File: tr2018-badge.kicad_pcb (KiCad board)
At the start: 2 copper layers, 70.4 x 53.3 mm, 16 parts, among them U1 ESP-12F, X1 Badgelife_shitty_connector

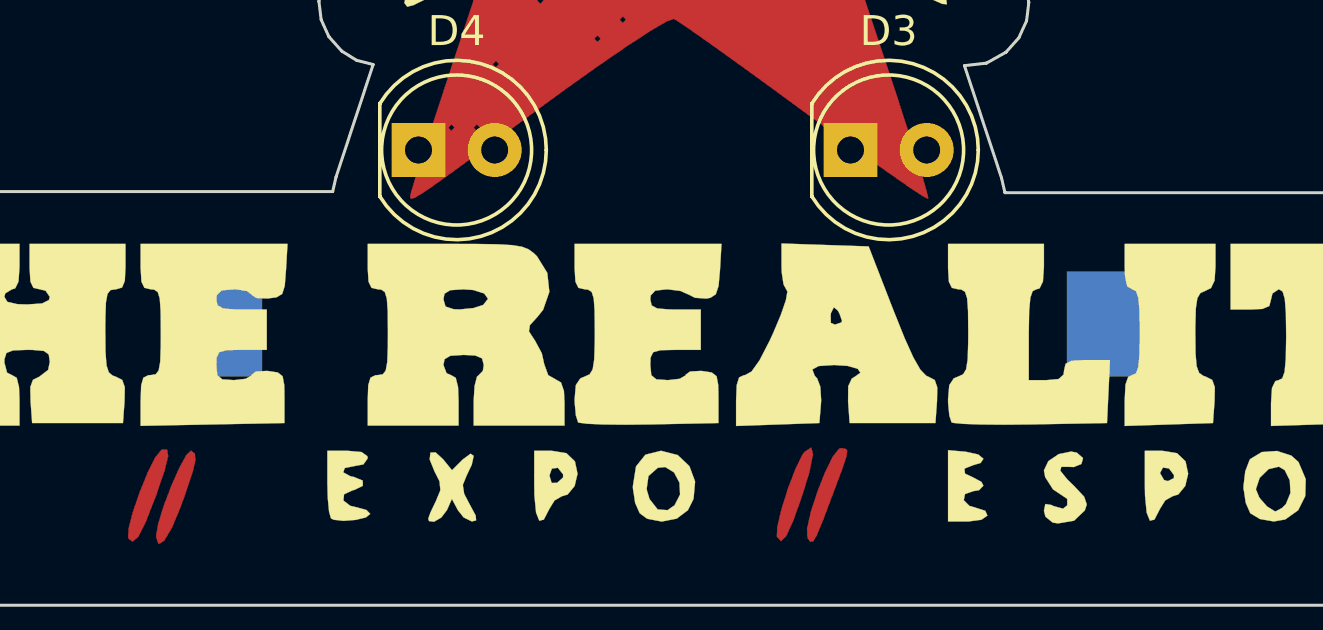
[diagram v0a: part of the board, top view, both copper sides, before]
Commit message: Updated schematic & design, added costs spreadsheet
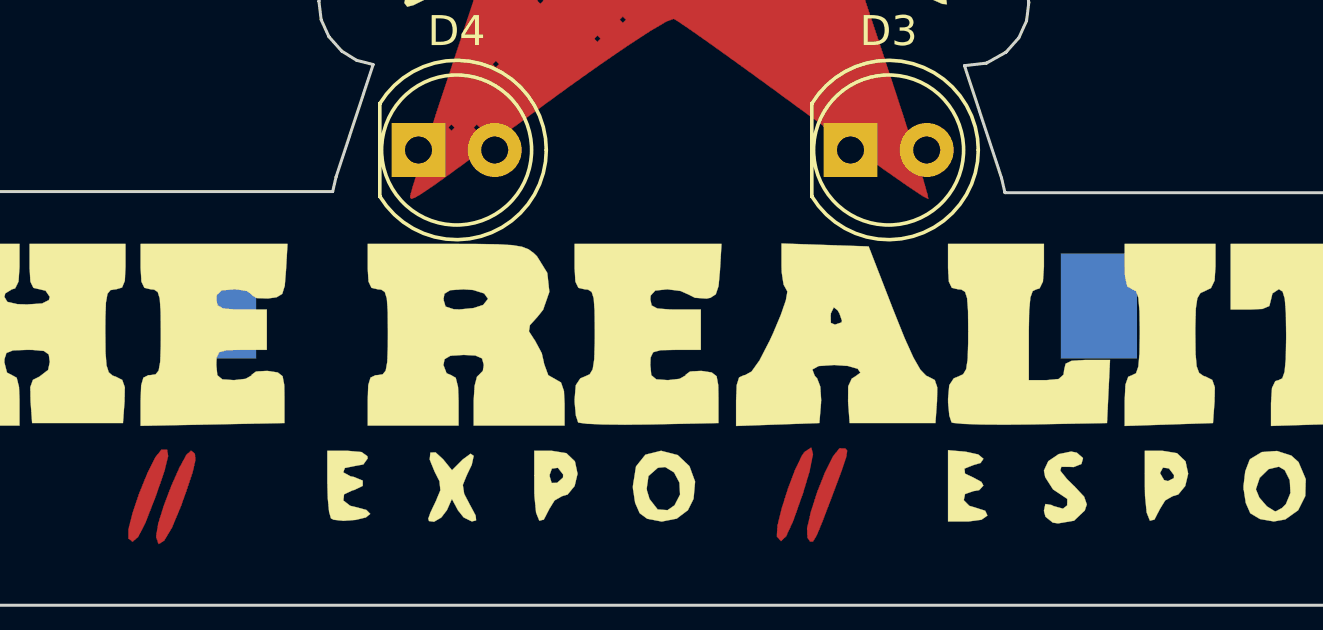
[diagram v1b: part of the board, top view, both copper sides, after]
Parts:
- moved BT1 0.63 mm to (52.0, 60.2)
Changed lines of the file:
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@@
     (pad_to_mask_clearance 0.2)
     (aux_axis_origin 0 0)
-    (visible_elements FFFFFF7F)
+    (visible_elements 7FFFFFFF)
     (pcbplotparams
       (layerselection 0x00030_80000001)
@@
   )
   (module Battery_Holders:Keystone_1058_1x2032-CoinCell (layer B.Cu)
-    (at 52.2 60.8 180)
+    (at 52 60.2 180)
     (descr http://www.keyelco.com/product-pdf.cfm?p=14028)
     (tags "Keystone type 1058 coin cell retainer")

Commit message: Added notes on PCB layout
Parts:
- D1: footprint LEDs:LED_D5.0mm -> LEDs:LED_D3.0mm
- moved D2 107.3 mm to (157.8, 91.4)
- moved D1 107.3 mm to (145.6, 82.4)
- moved R1 107.3 mm to (147.0, 84.4)
- moved R2 107.3 mm to (147.0, 86.2)
- moved R3 107.3 mm to (147.0, 88.0)
- moved U1 107.3 mm to (136.2, 81.0)
- moved X1 107.3 mm to (171.8, 113.0)
- moved BT1 107.3 mm to (146.6, 110.8)
- moved D3 107.3 mm to (153.0, 105.6)
- moved D4 107.3 mm to (138.6, 105.6)
- moved D5 107.3 mm to (134.2, 91.6)
- moved G*** 107.3 mm to (147.0, 94.6)
- moved G*** 107.3 mm to (147.0, 94.8)
- moved R4 107.3 mm to (147.0, 89.8)
- moved R5 107.3 mm to (147.0, 91.6)
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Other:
- board text added: "TODO: - Add version number on PCB - Add HackZone logo somewhere - Add names of contributors"

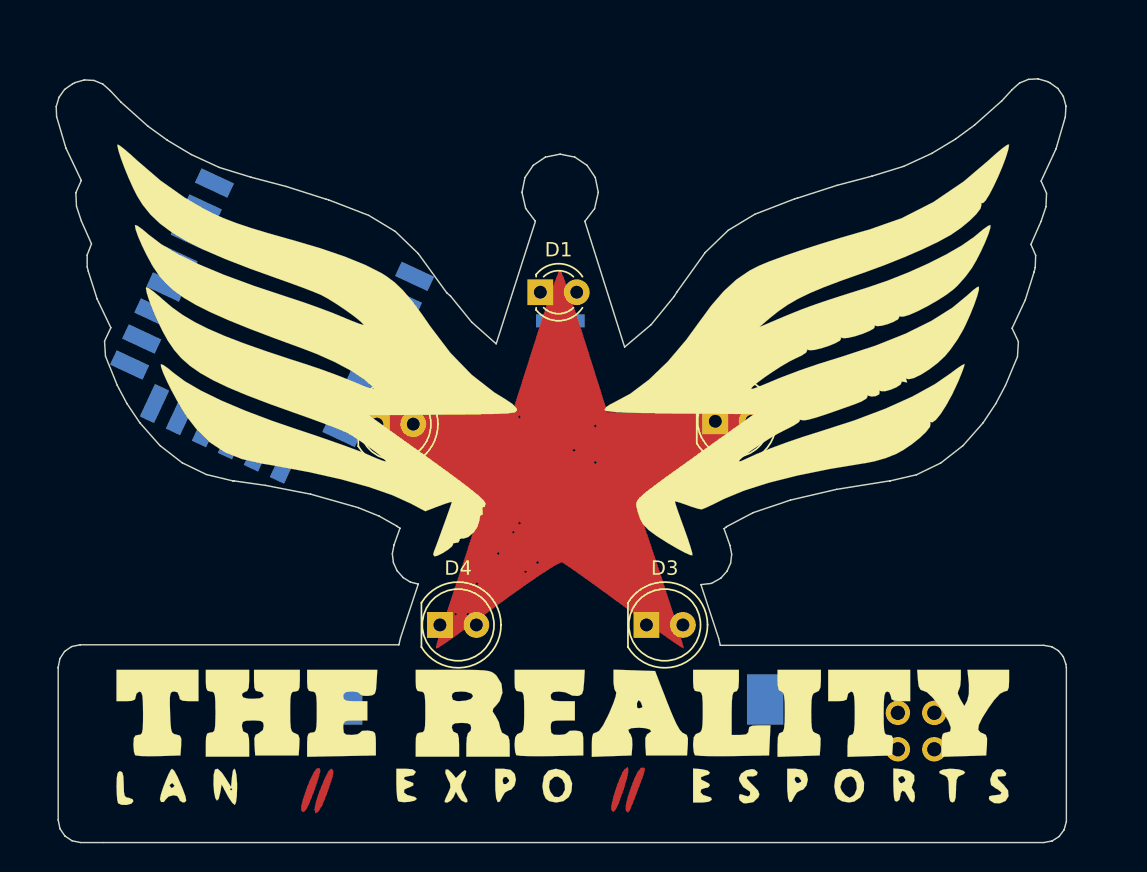
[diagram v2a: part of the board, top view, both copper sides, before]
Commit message: Updated badge design with latest ideas
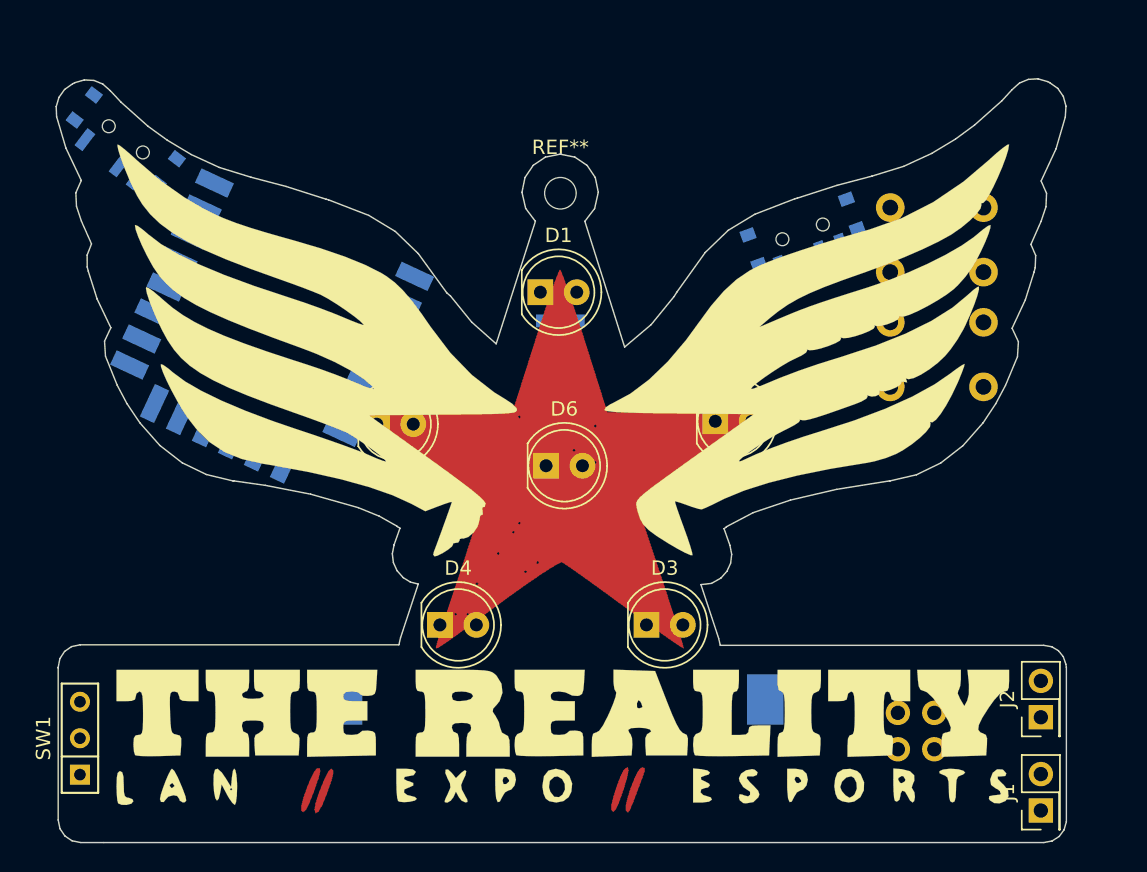
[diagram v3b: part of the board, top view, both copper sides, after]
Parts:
- added D6: LED, LEDs:LED_D5.0mm, F.Cu at (146.0, 94.5)
- added J1: Conn_02x01_Row_Letter_First, Pin_Headers:Pin_Header_Straight_2x01_Pitch2.54mm, F.Cu at (180.5, 118.5)
- added J2: Conn_02x01_Row_Letter_First, Pin_Headers:Pin_Header_Straight_2x01_Pitch2.54mm, F.Cu at (180.5, 112.0)
- added REF**: MountingHole_2.2mm_M2, Mounting_Holes:MountingHole_2.2mm_M2, F.Cu at (147.0, 75.5)
- added SW1: SW_SPDT, Buttons_Switches_THT:SW_Micro_SPST, F.Cu at (113.5, 113.5)
- added SW2: SW_SPDT, Buttons_Switches_SMD:SW_SPDT_PCM12, B.Cu at (116.5, 72.0)
- added SW3: SW_Push, Buttons_Switches_THT:SW_PUSH_6mm_h4.3mm, B.Cu at (176.5, 84.5)
- added SW4: SW_Push, Buttons_Switches_THT:SW_PUSH_6mm_h4.3mm, B.Cu at (170.0, 81.0)
- added SW5: SW_SPDT, Buttons_Switches_SMD:SW_SPDT_PCM12, B.Cu at (164.0, 78.5)
- D1: footprint LEDs:LED_D3.0mm -> LEDs:LED_D5.0mm
- renumbered G*** to COPPER, G*** to SILK
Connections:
- BT1 pad 2: GND -> Net-(BT1-Pad2)
- U1 pad 15: Net-(U1-Pad15) -> (no net)
- U1 pad 16: Net-(U1-Pad16) -> (no net)
- U1 pad 17: Net-(U1-Pad17) -> (no net)
- U1 pad 18: Net-(U1-Pad18) -> (no net)
- U1 pad 19: Net-(U1-Pad19) -> (no net)
- U1 pad 2: Net-(U1-Pad2) -> (no net)
- U1 pad 20: Net-(U1-Pad20) -> (no net)
- U1 pad 21: Net-(U1-Pad21) -> (no net)
- U1 pad 22: Net-(U1-Pad22) -> (no net)
- U1 pad 4: Net-(U1-Pad4) -> (no net)
- U1 pad 5: Net-(U1-Pad5) -> (no net)
- U1 pad 6: Net-(U1-Pad6) -> (no net)
- U1 pad 7: Net-(U1-Pad7) -> (no net)

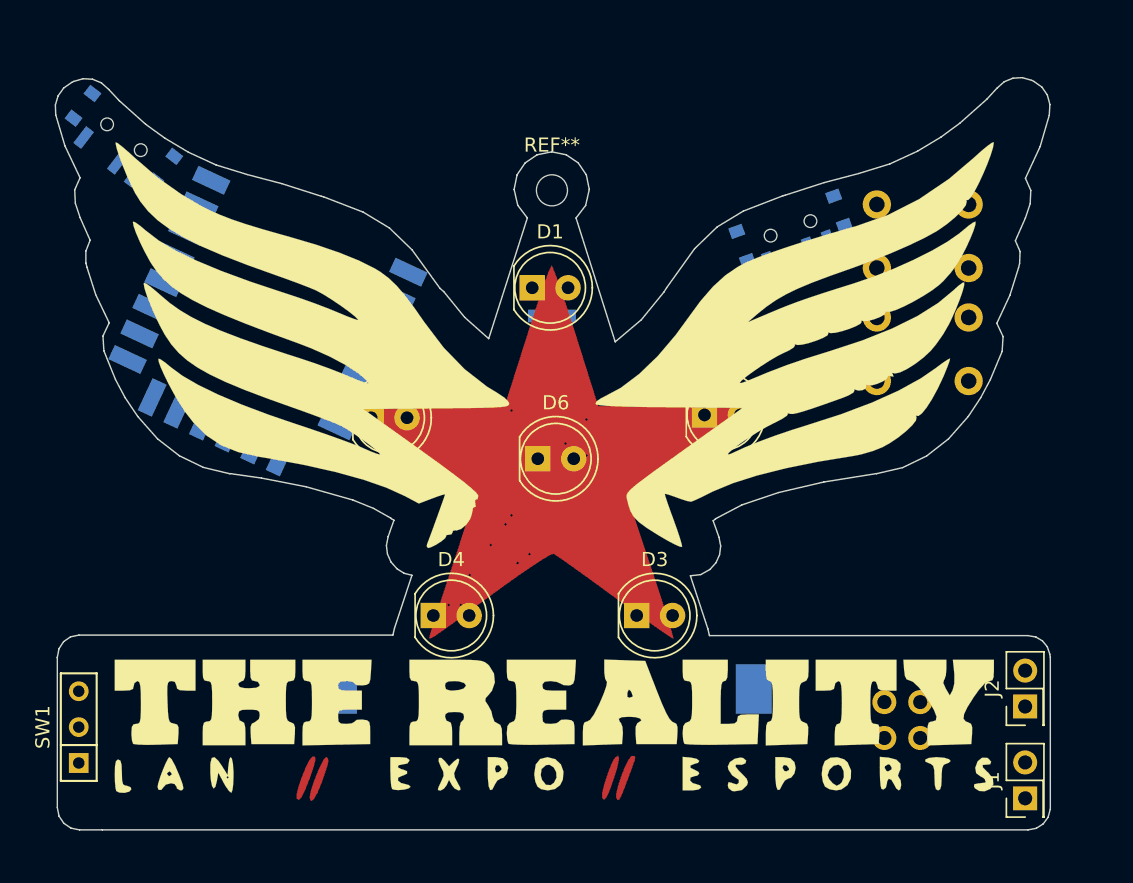
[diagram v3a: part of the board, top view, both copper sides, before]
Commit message: Design for PCB mill prototype (w/o functional ESP + SAO)
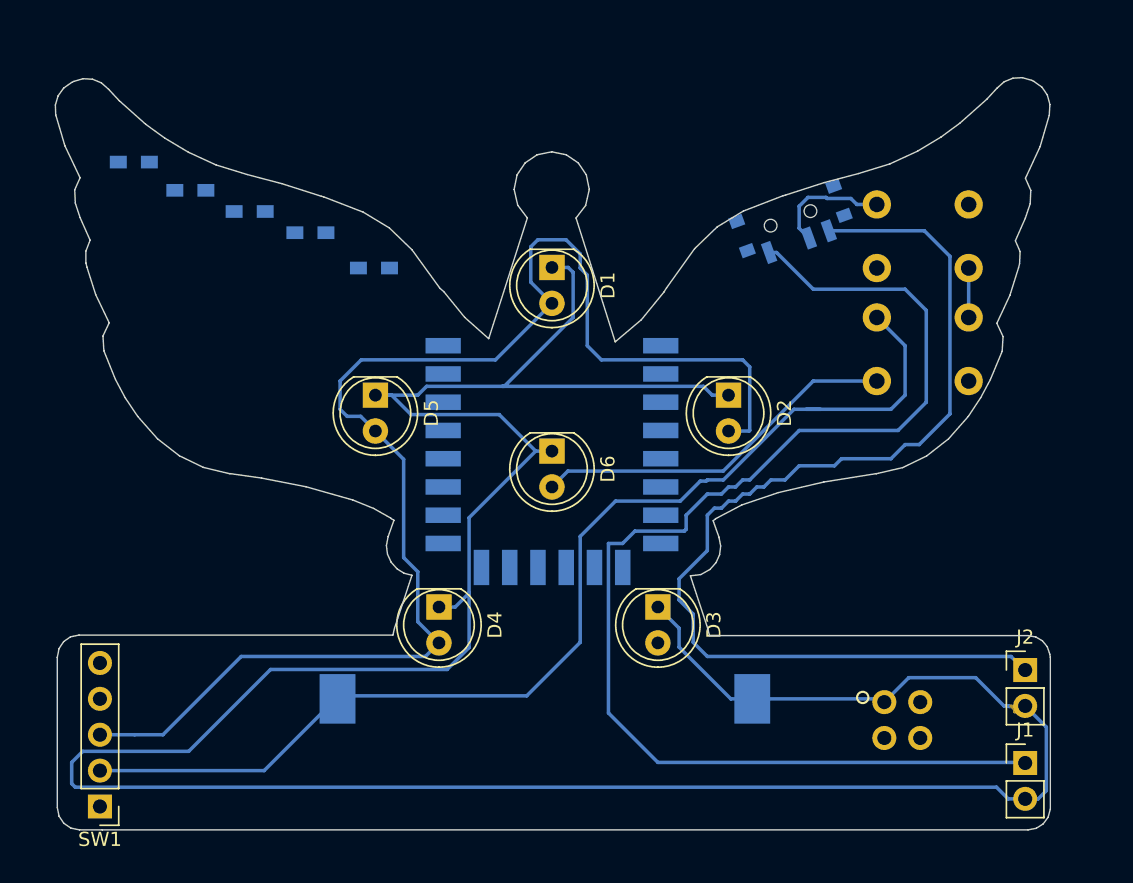
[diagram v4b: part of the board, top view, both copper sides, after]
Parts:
- removed COPPER: LOGO, modules:fill_cu
- removed REF**: MountingHole_2.2mm_M2, Mounting_Holes:MountingHole_2.2mm_M2
- removed SILK: LOGO, modules:wingstext
- removed STAR: LOGO, modules:fill
- removed SW2: SW_SPDT, Buttons_Switches_SMD:SW_SPDT_PCM12
- J1, J2: value Conn_02x01_Row_Letter_First -> Conn_01x02; footprint Pin_Headers:Pin_Header_Straight_2x01_Pitch2.54mm -> Pin_Headers:Pin_Header_Straight_1x02_Pitch2.54mm
- SW1: footprint Buttons_Switches_THT:SW_Micro_SPST -> Pin_Headers:Pin_Header_Straight_1x05_Pitch2.54mm
- moved R5 34.7 mm to (117.4, 73.5), turned to 180 degrees
- moved R4 29.3 mm to (121.4, 75.5), turned to 180 degrees
- moved R3 24.1 mm to (125.6, 77.0), turned to 180 degrees
- moved R2 18.8 mm to (129.9, 78.5), turned to 180 degrees
- moved U1 18.6 mm to (154.0, 86.5), turned to 180 degrees
- moved R1 13.1 mm to (134.4, 81.0)
- moved SW1 5.82 mm to (115.0, 119.1), turned to 180 degrees
- moved J2 2.58 mm to (180.5, 109.5), turned to 0 degrees
- moved J1 2.50 mm to (180.5, 116.0), turned to 0 degrees
- moved D2 2.20 mm to (159.5, 90.0), turned to 270 degrees
- moved D1 2.01 mm to (147.0, 81.0), turned to 270 degrees
- moved D5 1.63 mm to (134.5, 90.0), turned to 270 degrees
- moved D3 1.62 mm to (154.5, 105.0), turned to 270 degrees
- moved D6 1.14 mm to (147.0, 94.0), turned to 270 degrees
- moved D4 0.72 mm to (139.0, 105.0), turned to 270 degrees
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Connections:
- BT1 pad 2: Net-(BT1-Pad2) -> GND
- D1 pad 2: GND -> Net-(D1-Pad2)
- D2 pad 2: GND -> Net-(D1-Pad2)
- D3 pad 2: GND -> Net-(D1-Pad2)
- D4 pad 2: GND -> Net-(D1-Pad2)
- D5 pad 2: GND -> Net-(D1-Pad2)
- J1 pad 1: (no net) -> Net-(J1-Pad1)
- J1 pad 2: (no net) -> VCC
- J2 pad 1: (no net) -> Net-(J2-Pad1)
- J2 pad 2: (no net) -> VCC
- SW1 pad 2: Net-(SW1-Pad2) -> GND
- SW1 pad 3: Net-(BT1-Pad2) -> Net-(D1-Pad2)
- SW5 pad 1: (no net) -> Net-(J1-Pad1)
- SW5 pad 3: (no net) -> Net-(J2-Pad1)
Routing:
- net VCC: track 0.00 -> 210.4 mm
- net Net-(D1-Pad2): track 0.00 -> 99.6 mm
- net Net-(J1-Pad1): track 0.00 -> 89.5 mm
- net GND: track 0.00 -> 83.2 mm
- net Net-(J2-Pad1): track 0.00 -> 75.2 mm
- net Net-(D6-Pad2): track 0.00 -> 26.1 mm
- net Net-(SW4-Pad2): track 0.00 -> 8.50 mm
- net (no net): track 0.00 -> 0.72 mm

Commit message: Bump to rev 1.0.0
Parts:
- added G***: LOGO, modules:fill_mask, F.Cu at (147.0, 94.0)
- added REF**: MountingHole_2.2mm_M2_Pad_Via, Mounting_Holes:MountingHole_2.2mm_M2_Pad_Via, F.Cu at (147.0, 75.5)
- added Wings: LOGO, modules:wingstext, F.Cu at (147.0, 94.0)
- BT1: footprint Battery_Holders:Keystone_1058_1x2032-CoinCell -> BatteryHolder:Keystone_1058_1x2032-CoinCell
- J1, J2: moved to B.Cu
- R5: value 10k -> 10k (all opt.)
- SW1: footprint Pin_Headers:Pin_Header_Straight_1x05_Pitch2.54mm -> modules:SW_CuK_OS102011MA1QN1_SPDT_Angled; moved to B.Cu
- SW5 (opt.): renamed from SW5
- U1: value ESP-12F -> ESP-12F (opt.)
- X1: value Badgelife_shitty_connector -> Defcon Shitty AddOn (opt.) >
- moved X1 60.9 mm to (119.2, 82.3)
- moved SW1 43.7 mm to (124.2, 76.4), turned to 344 degrees
- moved J1 35.6 mm to (165.0, 84.0), turned to 90 degrees
- moved J2 26.9 mm to (165.0, 87.5), turned to 90 degrees
- moved R4 16.4 mm to (122.5, 91.9), turned to 270 degrees
- moved R5 15.2 mm to (119.5, 88.6), turned to 270 degrees
- moved R3 14.9 mm to (125.0, 91.9), turned to 270 degrees
- moved R2 13.6 mm to (127.5, 91.9), turned to 90 degrees
- moved R1 11.8 mm to (130.0, 91.9), turned to 90 degrees
- moved D4 0.50 mm to (139.5, 105.0)
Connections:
- SW1 pad 1: (no net) -> Net-(SW1-Pad1)
- U1 pad 15: (no net) -> Net-(U1-Pad15)
- U1 pad 16: (no net) -> Net-(U1-Pad16)
- U1 pad 17: (no net) -> Net-(U1-Pad17)
- U1 pad 18: (no net) -> Net-(U1-Pad18)
- U1 pad 19: (no net) -> Net-(U1-Pad19)
- U1 pad 2: (no net) -> Net-(U1-Pad2)
- U1 pad 20: (no net) -> Net-(U1-Pad20)
- U1 pad 21: (no net) -> Net-(U1-Pad21)
- U1 pad 22: (no net) -> Net-(U1-Pad22)
- U1 pad 4: (no net) -> Net-(U1-Pad4)
- U1 pad 5: (no net) -> Net-(U1-Pad5)
- U1 pad 6: (no net) -> Net-(U1-Pad6)
- U1 pad 7: (no net) -> Net-(U1-Pad7)
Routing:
- net Net-(J1-Pad1): track 89.5 -> 5.20 mm
- net VCC: track 210.4 -> 132.3 mm, vias 0 -> 1
- net Net-(J2-Pad1): track 75.2 -> 9.80 mm
- net GND: track 83.2 -> 126.2 mm, vias 0 -> 3
- net Net-(R1-Pad1): track 0.00 -> 32.7 mm, vias 0 -> 2
- net SDA: track 0.00 -> 30.8 mm, vias 0 -> 3
- net Net-(R2-Pad1): track 0.00 -> 29.6 mm
- net SCL: track 0.00 -> 26.4 mm, vias 0 -> 3
- net Net-(R5-Pad2): track 0.00 -> 24.9 mm, vias 0 -> 2
- net Net-(D1-Pad2): track 99.6 -> 76.8 mm, vias 0 -> 3
- net Net-(D6-Pad2): track 26.1 -> 48.4 mm, vias 0 -> 1
- net Net-(R4-Pad2): track 0.00 -> 18.9 mm
- net FLASH_EN: track 0.00 -> 17.1 mm
- net Net-(SW4-Pad2): track 8.50 -> 14.8 mm
- net (no net): track 0.72 -> 0.00 mm
- added copper zone on F.Cu, net GND
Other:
- board text added: "< all opt. ^"
- board text added: "Design & production by HackZone Rev 1.0.0"
- board text added: "The Reality Badge"
